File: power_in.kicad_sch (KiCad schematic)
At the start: 24 parts, among them Q17 AON7400, Q18 AON7400, Q19 MMBT5401, U16 LM5050-1, U17 LM5069

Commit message: POWER IN, OVLO, IDEAL DIODE
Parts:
- removed D11: 19-213/Y2C-CQ2R2L/3T(CY), LED_SMD:LED_0603_1608Metric_Pad1.05x0.95mm_HandSolder, symbol Device:LED
- removed Q17, Q18: AON7400, AON7408:TRANS_AON7408, symbol AON7408:AON7408
- removed R53: 10k, Resistor_SMD:R_0402_1005Metric, symbol Device:R_Small
- added Q1, Q2: FDMT80060DC, Package_TO_SOT_SMD:PQFN_8x8, symbol Transistor_FET:FDMT80060DC
- R28: value 22k -> 49k9
- R41: value 33k -> 18k
- R42: value 5.6k -> 12k1
- R48: value 25mR/1W -> 5mR/3W; footprint Resistor_SMD:R_1206_3216Metric -> Resistor_SMD:R_2512_6332Metric
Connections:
- net at C16.1, U16.4 (IN), U17.9 (OUT): now also Q1.2 (S), Q2.2 (S)
- net at D36.2 (A), R52.1, U17.10 (GATE): now also Q1.1 (G)
- net at R48.2, U17.1 (SENSE): now also Q1.3 (D)
- net PWR_IN: now reaches C19.2, C61.1, D1.1 (A1), R28.1, R48.1, U17.2 (VIN)
- net at U16.5 (GATE): now also Q2.1 (G)
- net +VSW renamed +12V
- net +12V: now also Q2.3 (D)
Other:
- note added: "OVLO"
- note removed: "power good"
- note removed: "softstart over current protection = 2A max UVLO = below 4V OVLP = over 27V"
- moved on the sheet: R48

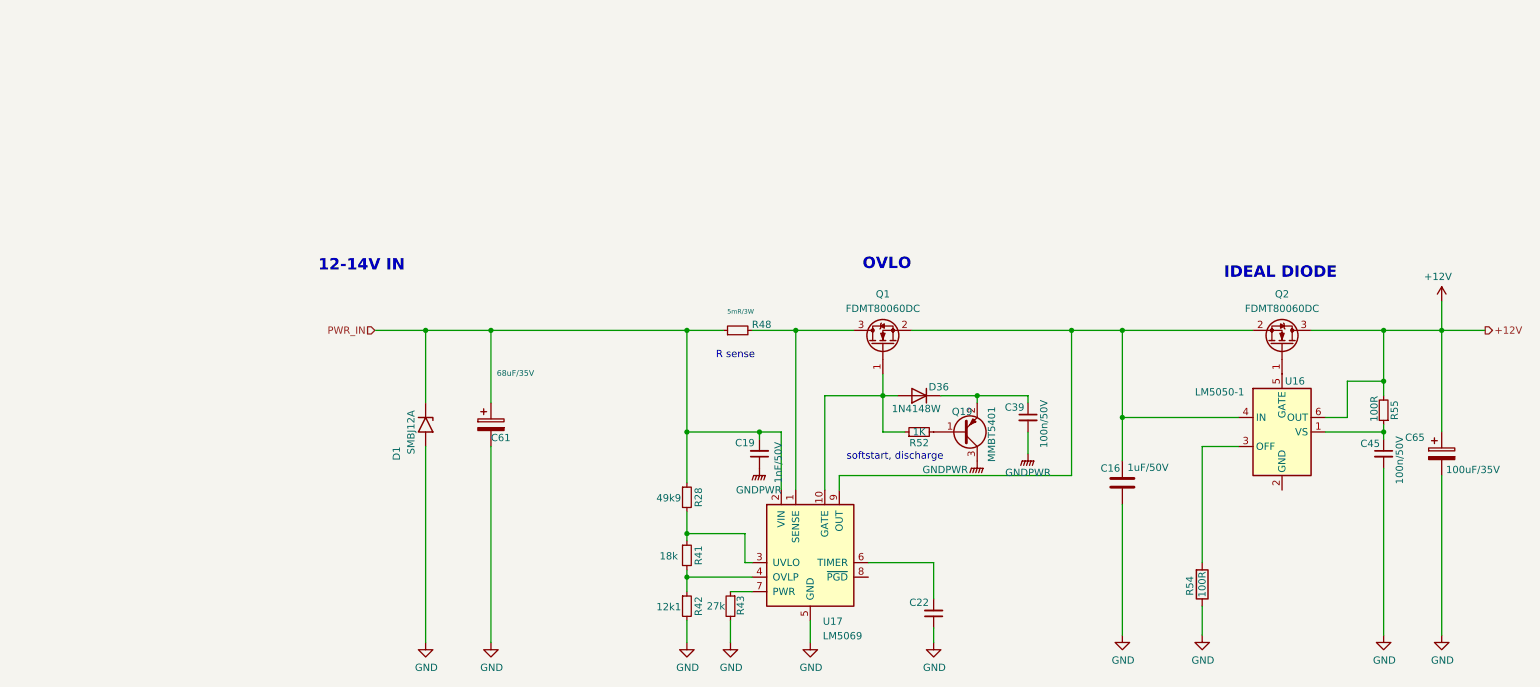
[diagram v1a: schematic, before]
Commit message: updated power stage placements
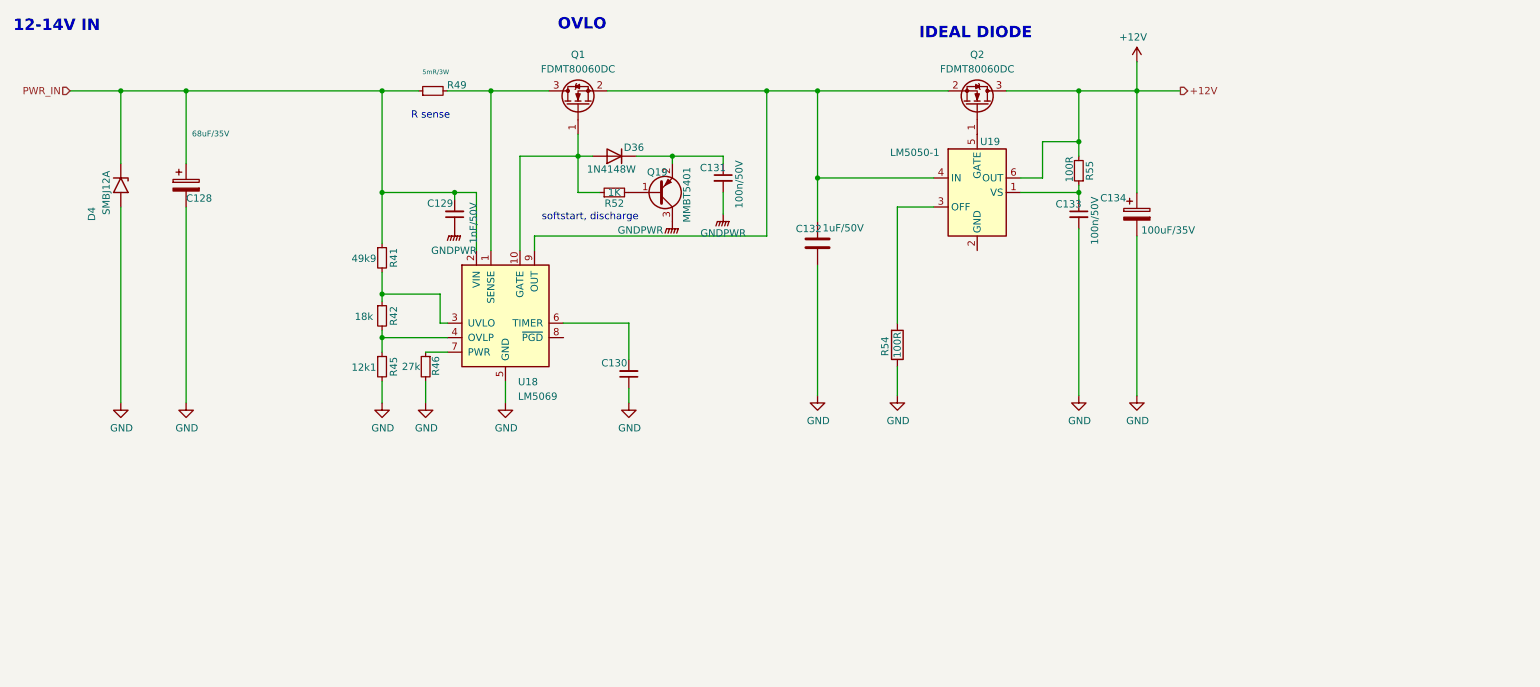
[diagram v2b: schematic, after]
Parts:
- removed C16: 1uF/50V, Capacitor_SMD:C_0603_1608Metric, symbol Device:C
- removed C19: 1nF/50V, Capacitor_SMD:C_0402_1005Metric, symbol Device:C_Small
- removed C22: 220nF/50V, Capacitor_SMD:C_0805_2012Metric, symbol Device:C_Small
- removed C39, C45: 100n/50V, Capacitor_SMD:C_0402_1005Metric, symbol Device:C_Small
- removed C61: 68uF/35V, Capacitor_SMD:CP_Elec_6.3x5.8, symbol Device:C_Polarized
- removed C65: 100uF/35V, Capacitor_SMD:CP_Elec_6.3x7.7, symbol Device:C_Polarized
- removed D1: SMBJ12A, Diode_SMD:D_SMB, symbol Diode:5KPxxA
- removed R28: 49k9, Resistor_SMD:R_0402_1005Metric, symbol Device:R_Small
- removed R43: 27k, Resistor_SMD:R_0402_1005Metric, symbol Device:R_Small
- removed R48: 5mR/3W, Resistor_SMD:R_2512_6332Metric, symbol Device:R_Small
- removed U16: LM5050-1, Package_TO_SOT_SMD:TSOT-23-6, symbol Power_Management:LM5050-1
- removed U17: LM5069, Package_SO:MSOP-10_3x3mm_P0.5mm, symbol lm5069:LM5069
- added C128: 68uF/35V, Capacitor_SMD:CP_Elec_6.3x5.8, symbol Device:C_Polarized
- added C129: 1nF/50V, Capacitor_SMD:C_0402_1005Metric, symbol Device:C_Small
- added C130: 220nF/50V, Capacitor_SMD:C_0805_2012Metric, symbol Device:C_Small
- added C131, C133: 100n/50V, Capacitor_SMD:C_0402_1005Metric, symbol Device:C_Small
- added C132: 1uF/50V, Capacitor_SMD:C_0603_1608Metric, symbol Device:C
- added C134: 100uF/35V, Capacitor_SMD:CP_Elec_6.3x7.7, symbol Device:C_Polarized
- added D4: SMBJ12A, Diode_SMD:D_SMB, symbol Diode:5KPxxA
- added R45: 12k1, Resistor_SMD:R_0402_1005Metric, symbol Device:R_Small
- added R46: 27k, Resistor_SMD:R_0402_1005Metric, symbol Device:R_Small
- added R49: 5mR/3W, Resistor_SMD:R_2512_6332Metric, symbol Device:R_Small
- added U18: LM5069, Package_SO:MSOP-10_3x3mm_P0.5mm, symbol lm5069:LM5069
- added U19: LM5050-1, Package_TO_SOT_SMD:TSOT-23-6, symbol Power_Management:LM5050-1
- R41: value 18k -> 49k9; footprint Resistor_SMD:R_0603_1608Metric -> Resistor_SMD:R_0402_1005Metric; LCSC C4216 -> C25768
- R42: value 12k1 -> 18k; footprint Resistor_SMD:R_0402_1005Metric -> Resistor_SMD:R_0603_1608Metric; LCSC C159996 -> C4216
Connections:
- net +12V: now also C134.1, U19.6 (OUT)
- net GND: now also C128.2, C130.1, C132.2, C133.2, C134.2, D4.2 (A2), R45.2, R46.2, U18.5 (GND); no longer R42.2
- net GNDPWR: now also C129.1, C131.2
- net PWR_IN: now also R41.1, C128.1, C129.2, D4.1 (A1), R49.1, U18.2 (VIN)
- net at D36.1 (K), Q19.2 (E): now also C131.1
- net at R54.2: now also U19.3 (OFF)
- net at Q2.1 (G): now also U19.5 (GATE)
- net at Q1.2 (S), Q2.2 (S): now also C132.1, U18.9 (OUT), U19.4 (IN)
- net at R55.1: now also C133.1, U19.1 (VS)
- net at R41.2, R42.1: now also U18.3 (UVLO)
- net at Q1.3 (D): now also R49.2, U18.1 (SENSE)
- net at D36.2 (A), Q1.1 (G), R52.1: now also U18.10 (GATE)
- new net: R46.1, U18.7 (PWR)
- new net: R42.2, R45.1, U18.4 (OVLP)
- new net: C130.2, U18.6 (TIMER)
